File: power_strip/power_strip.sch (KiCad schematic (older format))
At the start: 7 parts, among them J1 Barrel_Jack_Switch, J2 Battery, J3 Power, J4 Power, J5 Power, J6 Power, SW1 SW_DPDT_x2

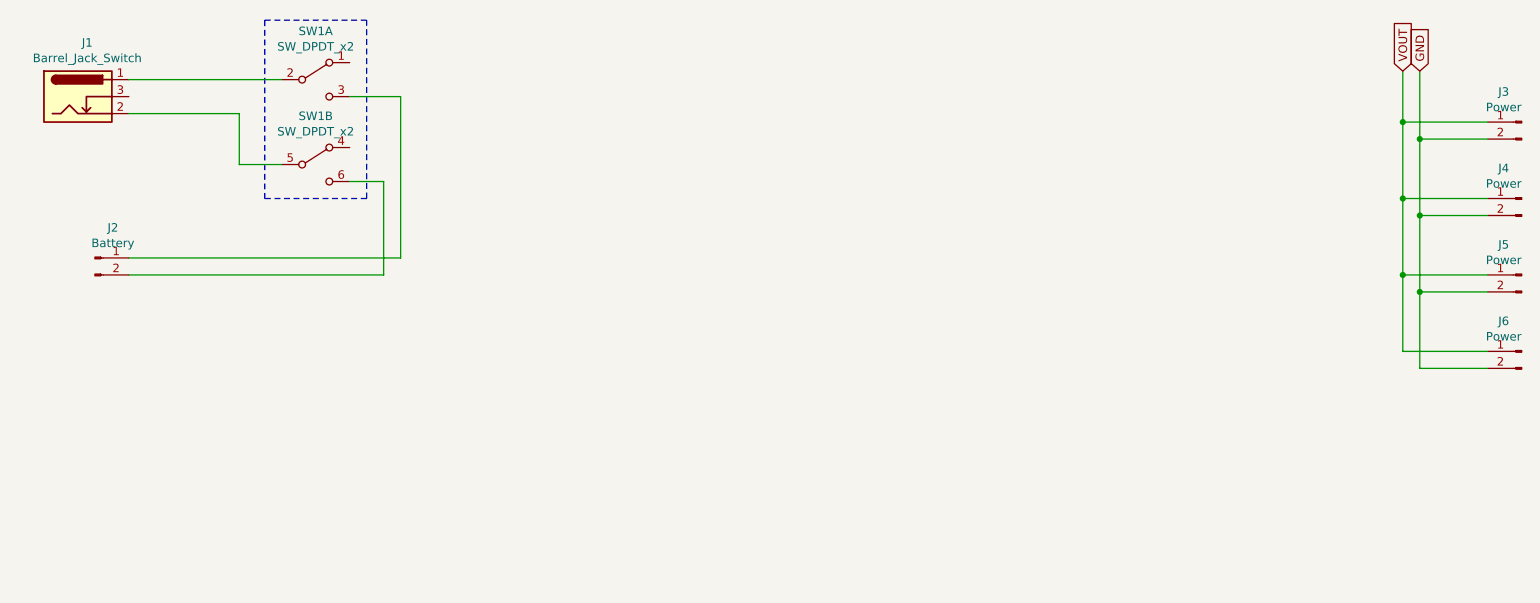
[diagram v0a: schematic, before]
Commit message: Update power strip. Circuit done
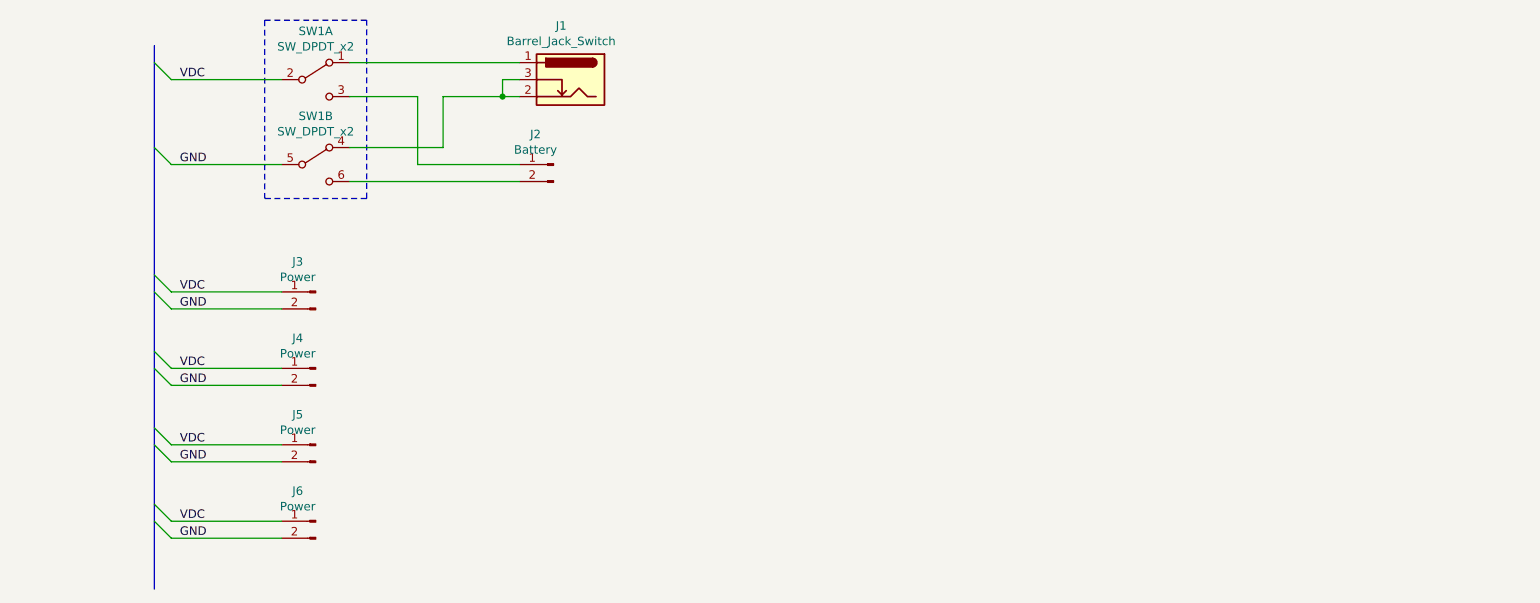
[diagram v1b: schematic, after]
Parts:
- J2, J3, J4, J5, J6: footprint (none) -> CATPOO:TerminalBlock_Pololu-2_P5.00mm
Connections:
- net VOUT is gone; now on net VDC: J3.1 (Pin_1), J4.1 (Pin_1), J5.1 (Pin_1), J6.1 (Pin_1)
- net GND: now also SW1.5 (B)
- net at SW1.1 (A): now also J1.1
- net VDC: now reaches SW1.2 (B)
- net VDC: no longer J1.1
- net at SW1.4 (A): now also J1.2, J1.3
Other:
- moved on the sheet: J1, J2, J3, J4, J5, J6
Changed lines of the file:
@@
 EESchema Schematic File Version 4
+LIBS:power_strip-cache
 EELAYER 26 0
 EELAYER END
@@
 L Connector:Conn_01x02_Male J2
 U 1 1 5C9DD72D
-P 1300 2800
-F 0 "J2" H 1406 2978 50  0000 C CNN
-F 1 "Battery" H 1406 2887 50  0000 C CNN
-F 2 "" H 1300 2800 50  0001 C CNN
-F 3 "~" H 1300 2800 50  0001 C CNN
-	1    1300 2800
-	1    0    0    -1
+P 4000 2250
+F 0 "J2" H 4106 2428 50  0000 C CNN
+F 1 "Battery" H 4106 2337 50  0000 C CNN
+F 2 "CATPOO:TerminalBlock_Pololu-2_P5.00mm" H 4000 2250 50  0001 C CNN
+F 3 "~" H 4000 2250 50  0001 C CNN
+	1    4000 2250
+	-1   0    0    -1
 $EndComp
 $Comp
 L Connector:Conn_01x02_Male J3
 U 1 1 5C9DD850
-P 9700 2000
-F 0 "J3" H 9806 2178 50  0000 C CNN
-F 1 "Power" H 9806 2087 50  0000 C CNN
-F 2 "" H 9700 2000 50  0001 C CNN
-F 3 "~" H 9700 2000 50  0001 C CNN
-	1    9700 2000
+P 2600 3000
+F 0 "J3" H 2706 3178 50  0000 C CNN
+F 1 "Power" H 2706 3087 50  0000 C CNN
+F 2 "CATPOO:TerminalBlock_Pololu-2_P5.00mm" H 2600 3000 50  0001 C CNN
+F 3 "~" H 2600 3000 50  0001 C CNN
+	1    2600 3000
 	-1   0    0    -1
 $EndComp
@@
 L Connector:Conn_01x02_Male J4
 U 1 1 5C9DD8C0
-P 9700 2450
-F 0 "J4" H 9806 2628 50  0000 C CNN
-F 1 "Power" H 9806 2537 50  0000 C CNN
-F 2 "" H 9700 2450 50  0001 C CNN
-F 3 "~" H 9700 2450 50  0001 C CNN
-	1    9700 2450
+P 2600 3450
+F 0 "J4" H 2706 3628 50  0000 C CNN
+F 1 "Power" H 2706 3537 50  0000 C CNN
+F 2 "CATPOO:TerminalBlock_Pololu-2_P5.00mm" H 2600 3450 50  0001 C CNN
+F 3 "~" H 2600 3450 50  0001 C CNN
+	1    2600 3450
 	-1   0    0    -1
 $EndComp
@@
 L Connector:Conn_01x02_Male J5
 U 1 1 5C9DD91A
-P 9700 2900
-F 0 "J5" H 9806 3078 50  0000 C CNN
-F 1 "Power" H 9806 2987 50  0000 C CNN
-F 2 "" H 9700 2900 50  0001 C CNN
-F 3 "~" H 9700 2900 50  0001 C CNN
-	1    9700 2900
+P 2600 3900
+F 0 "J5" H 2706 4078 50  0000 C CNN
+F 1 "Power" H 2706 3987 50  0000 C CNN
+F 2 "CATPOO:TerminalBlock_Pololu-2_P5.00mm" H 2600 3900 50  0001 C CNN
+F 3 "~" H 2600 3900 50  0001 C CNN
+	1    2600 3900
 	-1   0    0    -1
 $EndComp
@@
 L Connector:Conn_01x02_Male J6
 U 1 1 5C9DD946
-P 9700 3350
-F 0 "J6" H 9806 3528 50  0000 C CNN
-F 1 "Power" H 9806 3437 50  0000 C CNN
-F 2 "" H 9700 3350 50  0001 C CNN
-F 3 "~" H 9700 3350 50  0001 C CNN
-	1    9700 3350
+P 2600 4350
+F 0 "J6" H 2706 4528 50  0000 C CNN
+F 1 "Power" H 2706 4437 50  0000 C CNN
+F 2 "CATPOO:TerminalBlock_Pololu-2_P5.00mm" H 2600 4350 50  0001 C CNN
+F 3 "~" H 2600 4350 50  0001 C CNN
+	1    2600 4350
 	-1   0    0    -1
 $EndComp
@@
 	1    0    0    -1
 $EndComp
-Wire Wire Line
-	2150 2250 2400 2250
 Wire Notes Line
 	2300 1400 2300 2450
@@
 Wire Notes Line
 	2300 1400 2900 1400
-Wire Wire Line
-	2800 2350 3000 2350
-Wire Wire Line
-	3000 2350 3000 2900
-Wire Wire Line
-	3000 2900 1500 2900
-Wire Wire Line
-	2800 1850 3100 1850
-Wire Wire Line
-	3100 1850 3100 2800
-Wire Wire Line
-	3100 2800 1500 2800
-Wire Wire Line
-	9000 2000 9500 2000
-Wire Wire Line
-	9500 2100 9100 2100
-Wire Wire Line
-	9500 2550 9100 2550
-Wire Wire Line
-	9100 2100 9100 2550
-Wire Wire Line
-	9100 3450 9500 3450
-Connection ~ 9100 2550
-Wire Wire Line
-	9100 2550 9100 3000
-Wire Wire Line
-	9500 3000 9100 3000
-Connection ~ 9100 3000
-Wire Wire Line
-	9100 3000 9100 3450
-Wire Wire Line
-	9500 3350 9000 3350
-Wire Wire Line
-	9000 3350 9000 2900
-Wire Wire Line
-	9500 2450 9000 2450
-Connection ~ 9000 2450
-Wire Wire Line
-	9000 2450 9000 2000
-Wire Wire Line
-	9500 2900 9000 2900
-Connection ~ 9000 2900
-Wire Wire Line
-	9000 2900 9000 2450
-Text GLabel 9000 1700 1    50   Input ~ 0
-VOUT
-Wire Wire Line
-	9000 1700 9000 2000
-Connection ~ 9000 2000
-Text GLabel 9100 1700 1    50   Input ~ 0
-GND
-Wire Wire Line
-	9100 1700 9100 2100
-Connection ~ 9100 2100
 $Comp
 L Connector:Barrel_Jack_Switch J1
 U 1 1 5C9E579F
-P 1200 1850
-F 0 "J1" H 1255 2167 50  0000 C CNN
-F 1 "Barrel_Jack_Switch" H 1255 2076 50  0000 C CNN
-F 2 "" H 1250 1810 50  0001 C CNN
-F 3 "~" H 1250 1810 50  0001 C CNN
-	1    1200 1850
-	1    0    0    -1
+P 4100 1750
+F 0 "J1" H 4155 2067 50  0000 C CNN
+F 1 "Barrel_Jack_Switch" H 4155 1976 50  0000 C CNN
+F 2 "" H 4150 1710 50  0001 C CNN
+F 3 "~" H 4150 1710 50  0001 C CNN
+	1    4100 1750
+	-1   0    0    -1
 $EndComp
 Wire Wire Line
-	1500 1950 2150 1950
+	3800 1750 3700 1750
 Wire Wire Line
-	2150 1950 2150 2250
+	3700 1750 3700 1850
 Wire Wire Line
-	1500 1750 2400 1750
+	3700 1850 3800 1850
+Wire Wire Line
+	2800 1650 3800 1650
+Wire Wire Line
+	2800 2150 3350 2150
+Wire Wire Line
+	3350 2150 3350 1850
+Wire Wire Line
+	3350 1850 3700 1850
+Connection ~ 3700 1850
+Wire Wire Line
+	2800 1850 3200 1850
+Wire Wire Line
+	3200 1850 3200 2250
+Wire Wire Line
+	3200 2250 3800 2250
+Wire Wire Line
+	2800 2350 3800 2350
+Entry Wire Line
+	1650 1650 1750 1750
+Entry Wire Line
+	1650 2150 1750 2250
+Entry Wire Line
+	1650 2900 1750 3000
+Entry Wire Line
+	1650 3000 1750 3100
+Entry Wire Line
+	1650 3350 1750 3450
+Entry Wire Line
+	1650 3450 1750 3550
+Entry Wire Line
+	1650 3800 1750 3900
+Entry Wire Line
+	1650 3900 1750 4000
+Wire Wire Line
+	1750 1750 2400 1750
+Wire Wire Line
+	2400 2250 1750 2250
+Text Label 1800 2250 0    50   ~ 0
+GND
+Text Label 1800 1750 0    50   ~ 0
+VDC
+Wire Wire Line
+	2400 3000 1750 3000
+Wire Wire Line
+	1750 3100 2400 3100
+Wire Wire Line
+	2400 3450 1750 3450
+Wire Wire Line
+	1750 3550 2400 3550
+Wire Wire Line
+	2400 3900 1750 3900
+Wire Wire Line
+	1750 4000 2400 4000
+Entry Wire Line
+	1650 4250 1750 4350
+Entry Wire Line
+	1650 4350 1750 4450
+Wire Wire Line
+	1750 4350 2400 4350
+Wire Wire Line
+	1750 4450 2400 4450
+Wire Bus Line
+	1650 1550 1650 4750
+Text Label 1800 3100 0    50   ~ 0
+GND
+Text Label 1800 3550 0    50   ~ 0
+GND
+Text Label 1800 4000 0    50   ~ 0
+GND
+Text Label 1800 4450 0    50   ~ 0
+GND
+Text Label 1800 3000 0    50   ~ 0
+VDC
+Text Label 1800 3450 0    50   ~ 0
+VDC
+Text Label 1800 3900 0    50   ~ 0
+VDC
+Text Label 1800 4350 0    50   ~ 0
+VDC
 $EndSCHEMATC

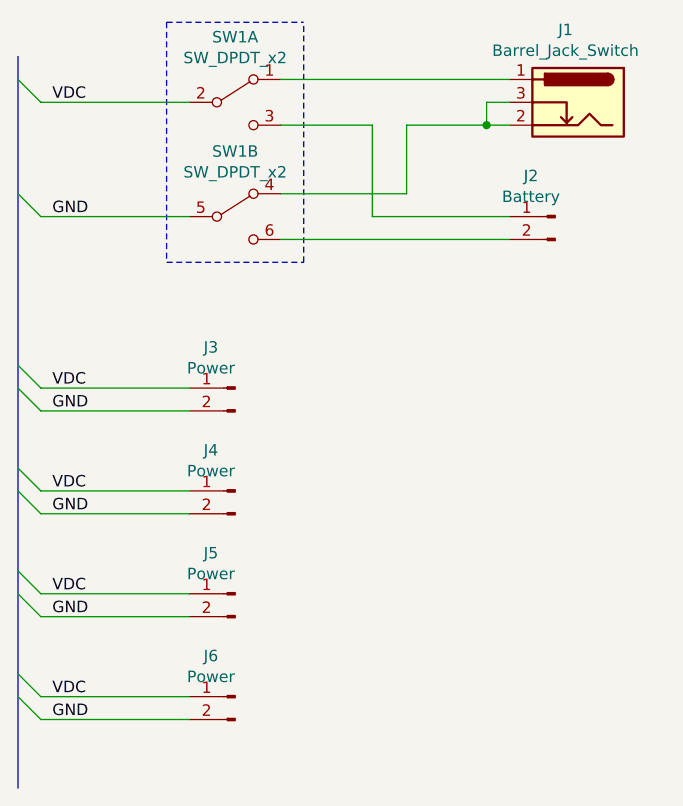
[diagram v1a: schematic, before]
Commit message: Finish power strip
It now only does exactly what it needs to do, and that's
split an incoming power into 3 other outputs.
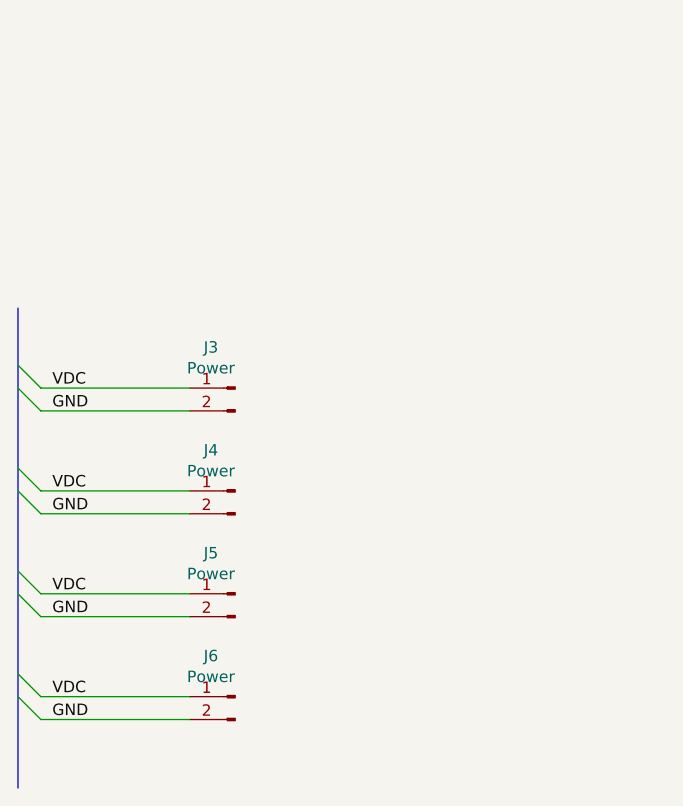
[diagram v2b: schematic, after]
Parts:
- removed J1: Barrel_Jack_Switch, symbol Connector:Barrel_Jack_Switch
- removed J2: Battery, CATPOO:TerminalBlock_Pololu-2_P5.00mm, symbol Connector:Conn_01x02_Male
- removed SW1: SW_DPDT_x2, symbol Switch:SW_DPDT_x2
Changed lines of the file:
@@
 $EndDescr
-$Comp
-L Connector:Conn_01x02_Male J2
-U 1 1 5C9DD72D
-P 4000 2250
-F 0 "J2" H 4106 2428 50  0000 C CNN
-F 1 "Battery" H 4106 2337 50  0000 C CNN
-F 2 "CATPOO:TerminalBlock_Pololu-2_P5.00mm" H 4000 2250 50  0001 C CNN
-F 3 "~" H 4000 2250 50  0001 C CNN
-	1    4000 2250
-	-1   0    0    -1
-$EndComp
 $Comp
 L Connector:Conn_01x02_Male J3
@@
 	-1   0    0    -1
 $EndComp
-$Comp
-L Switch:SW_DPDT_x2 SW1
-U 2 1 5C9DE0BA
-P 2600 2250
-F 0 "SW1" H 2600 2535 50  0000 C CNN
-F 1 "SW_DPDT_x2" H 2600 2444 50  0000 C CNN
-F 2 "" H 2600 2250 50  0001 C CNN
-F 3 "" H 2600 2250 50  0001 C CNN
-	2    2600 2250
-	1    0    0    -1
-$EndComp
-$Comp
-L Switch:SW_DPDT_x2 SW1
-U 1 1 5C9DE02A
-P 2600 1750
-F 0 "SW1" H 2600 2035 50  0000 C CNN
-F 1 "SW_DPDT_x2" H 2600 1944 50  0000 C CNN
-F 2 "" H 2600 1750 50  0001 C CNN
-F 3 "" H 2600 1750 50  0001 C CNN
-	1    2600 1750
-	1    0    0    -1
-$EndComp
-Wire Notes Line
-	2300 1400 2300 2450
-Wire Notes Line
-	2300 2450 2900 2450
-Wire Notes Line
-	2900 2450 2900 1400
-Wire Notes Line
-	2300 1400 2900 1400
-$Comp
-L Connector:Barrel_Jack_Switch J1
-U 1 1 5C9E579F
-P 4100 1750
-F 0 "J1" H 4155 2067 50  0000 C CNN
-F 1 "Barrel_Jack_Switch" H 4155 1976 50  0000 C CNN
-F 2 "" H 4150 1710 50  0001 C CNN
-F 3 "~" H 4150 1710 50  0001 C CNN
-	1    4100 1750
-	-1   0    0    -1
-$EndComp
-Wire Wire Line
-	3800 1750 3700 1750
-Wire Wire Line
-	3700 1750 3700 1850
-Wire Wire Line
-	3700 1850 3800 1850
-Wire Wire Line
-	2800 1650 3800 1650
-Wire Wire Line
-	2800 2150 3350 2150
-Wire Wire Line
-	3350 2150 3350 1850
-Wire Wire Line
-	3350 1850 3700 1850
-Connection ~ 3700 1850
-Wire Wire Line
-	2800 1850 3200 1850
-Wire Wire Line
-	3200 1850 3200 2250
-Wire Wire Line
-	3200 2250 3800 2250
-Wire Wire Line
-	2800 2350 3800 2350
-Entry Wire Line
-	1650 1650 1750 1750
-Entry Wire Line
-	1650 2150 1750 2250
 Entry Wire Line
 	1650 2900 1750 3000
@@
 Entry Wire Line
 	1650 3900 1750 4000
-Wire Wire Line
-	1750 1750 2400 1750
-Wire Wire Line
-	2400 2250 1750 2250
-Text Label 1800 2250 0    50   ~ 0
-GND
-Text Label 1800 1750 0    50   ~ 0
-VDC
 Wire Wire Line
 	2400 3000 1750 3000
@@
 Wire Wire Line
 	1750 4450 2400 4450
-Wire Bus Line
-	1650 1550 1650 4750
 Text Label 1800 3100 0    50   ~ 0
 GND
@@
 Text Label 1800 4350 0    50   ~ 0
 VDC
+Wire Bus Line
+	1650 2650 1650 4750
 $EndSCHEMATC
